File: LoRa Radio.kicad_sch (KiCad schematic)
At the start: 19 parts, among them U10 SX1262IMLTRT, U5 SKY66105, U9 74LVC2T45DC, Y2 ATX-11-F-32.000MHZ-F05-T

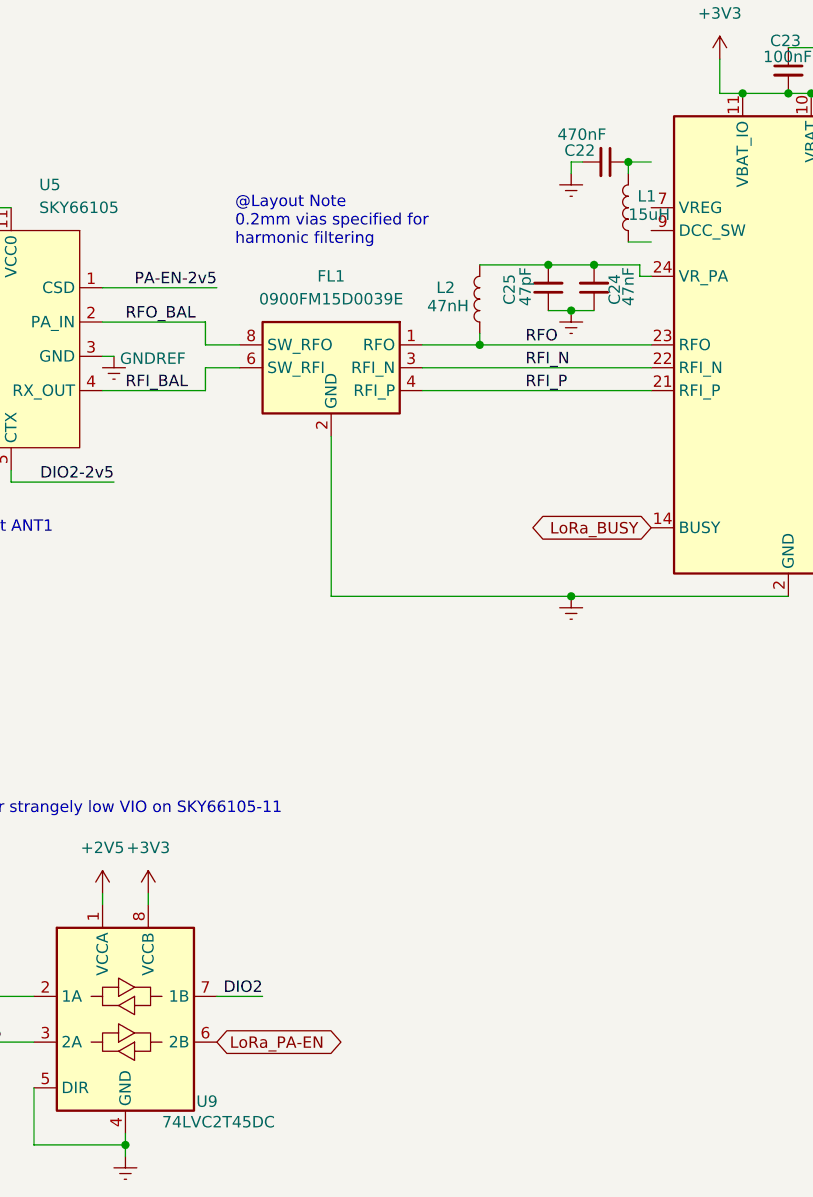
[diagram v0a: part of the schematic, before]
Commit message: Fix footprints and update rev number
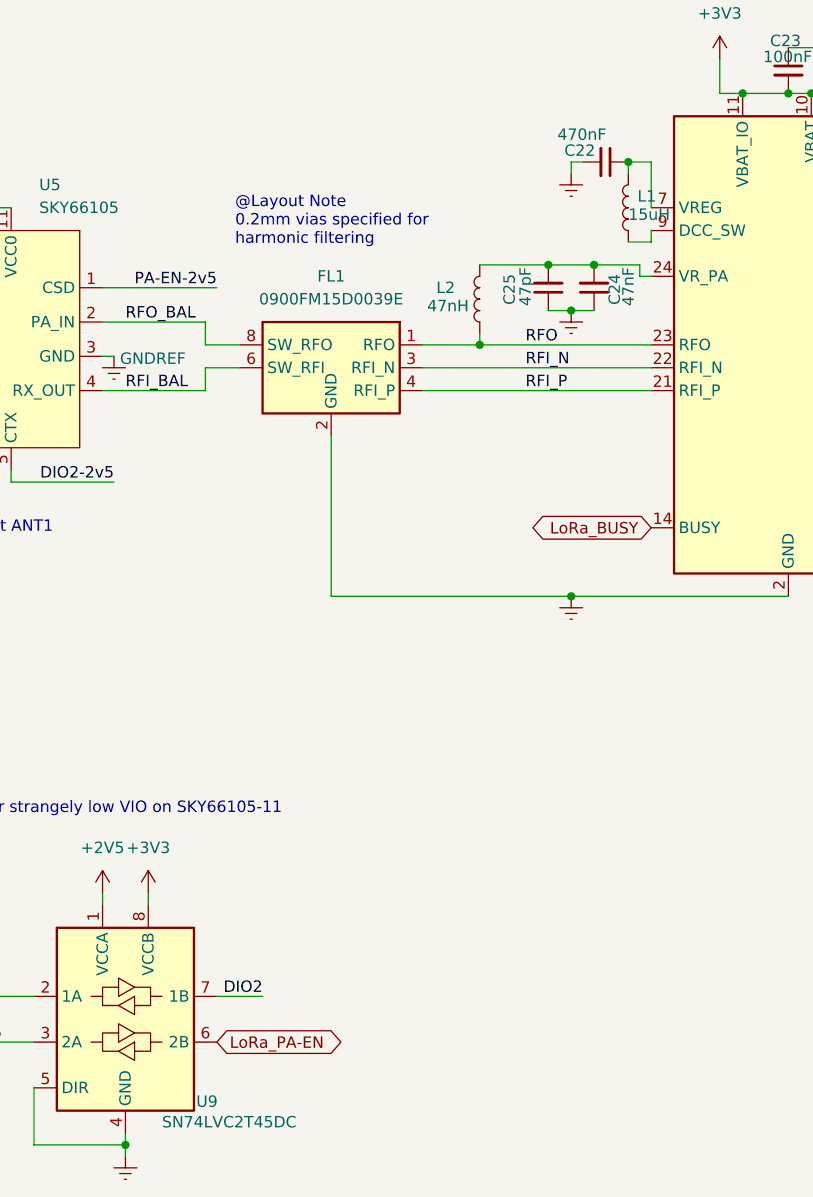
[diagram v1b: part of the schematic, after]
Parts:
- U9: value 74LVC2T45DC -> SN74LVC2T45DC; footprint Package_SO:VSSOP-8_2.3x2mm_P0.5mm -> Package_SO:MSOP-8_3x3mm_P0.65mm
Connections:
- net at U10.7 (VREG): now also C22.1, L1.2
- net at U10.9 (DCC_SW): now also L1.1
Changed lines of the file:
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@@
 	(title_block
 		(title "WINTER 915MHz LoRa Radio")
-		(date "2025-01-06")
-		(rev "3.3")
+		(date "2025-08-28")
+		(rev "4-Dev")
 		(company "SparrowTheNerd")
 	)
@@
 	(wire
 		(pts
+			(xy 149.86 60.96) (xy 149.86 66.04)
+		)
+		(stroke
+			(width 0)
+			(type default)
+		)
+	)
+	(wire
+		(pts
 			(xy 68.58 153.67) (xy 81.28 153.67)
 		)
@@
 	(wire
 		(pts
+			(xy 149.86 68.58) (xy 149.86 69.85)
+		)
+		(stroke
+			(width 0)
+			(type default)
+		)
+	)
+	(wire
+		(pts
 			(xy 88.9 74.93) (xy 101.6 74.93)
 		)
@@
 			)
 		)
-		(property "Value" "74LVC2T45DC"
+		(property "Value" "SN74LVC2T45DC"
 			(at 95.504 167.64 0)
 			(effects
@@
 			)
 		)
-		(property "Footprint" "Package_SO:VSSOP-8_2.3x2mm_P0.5mm"
+		(property "Footprint" "Package_SO:MSOP-8_3x3mm_P0.65mm"
 			(at 91.44 177.8 0)
 			(effects

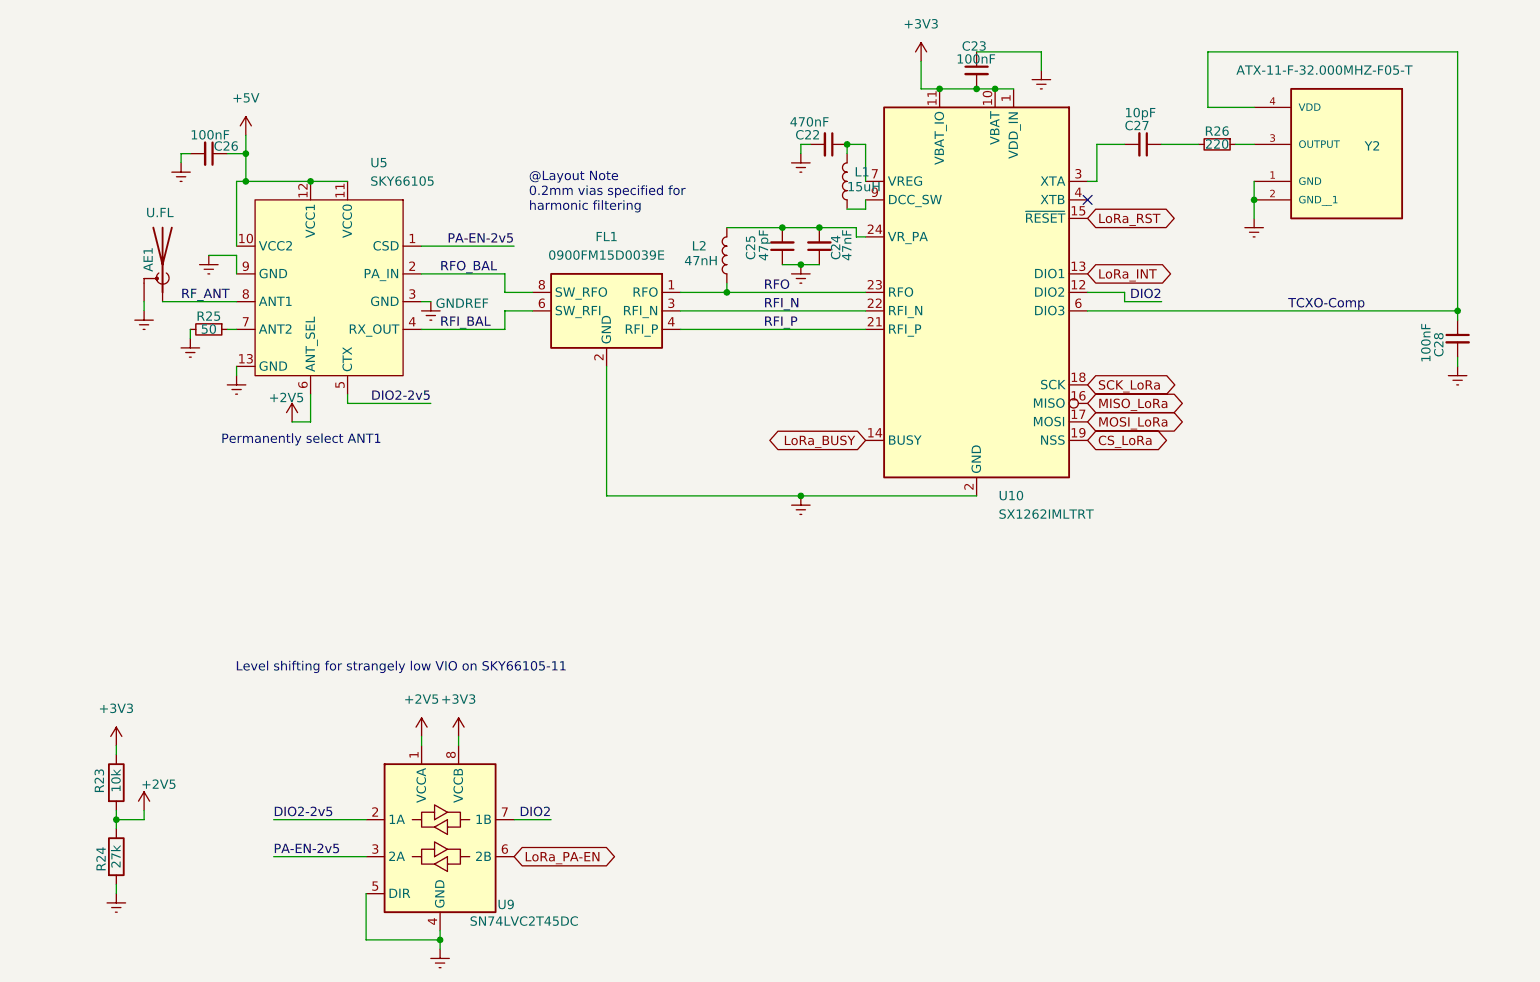
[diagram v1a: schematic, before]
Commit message: updated power delivery and component choices. v4 now ready
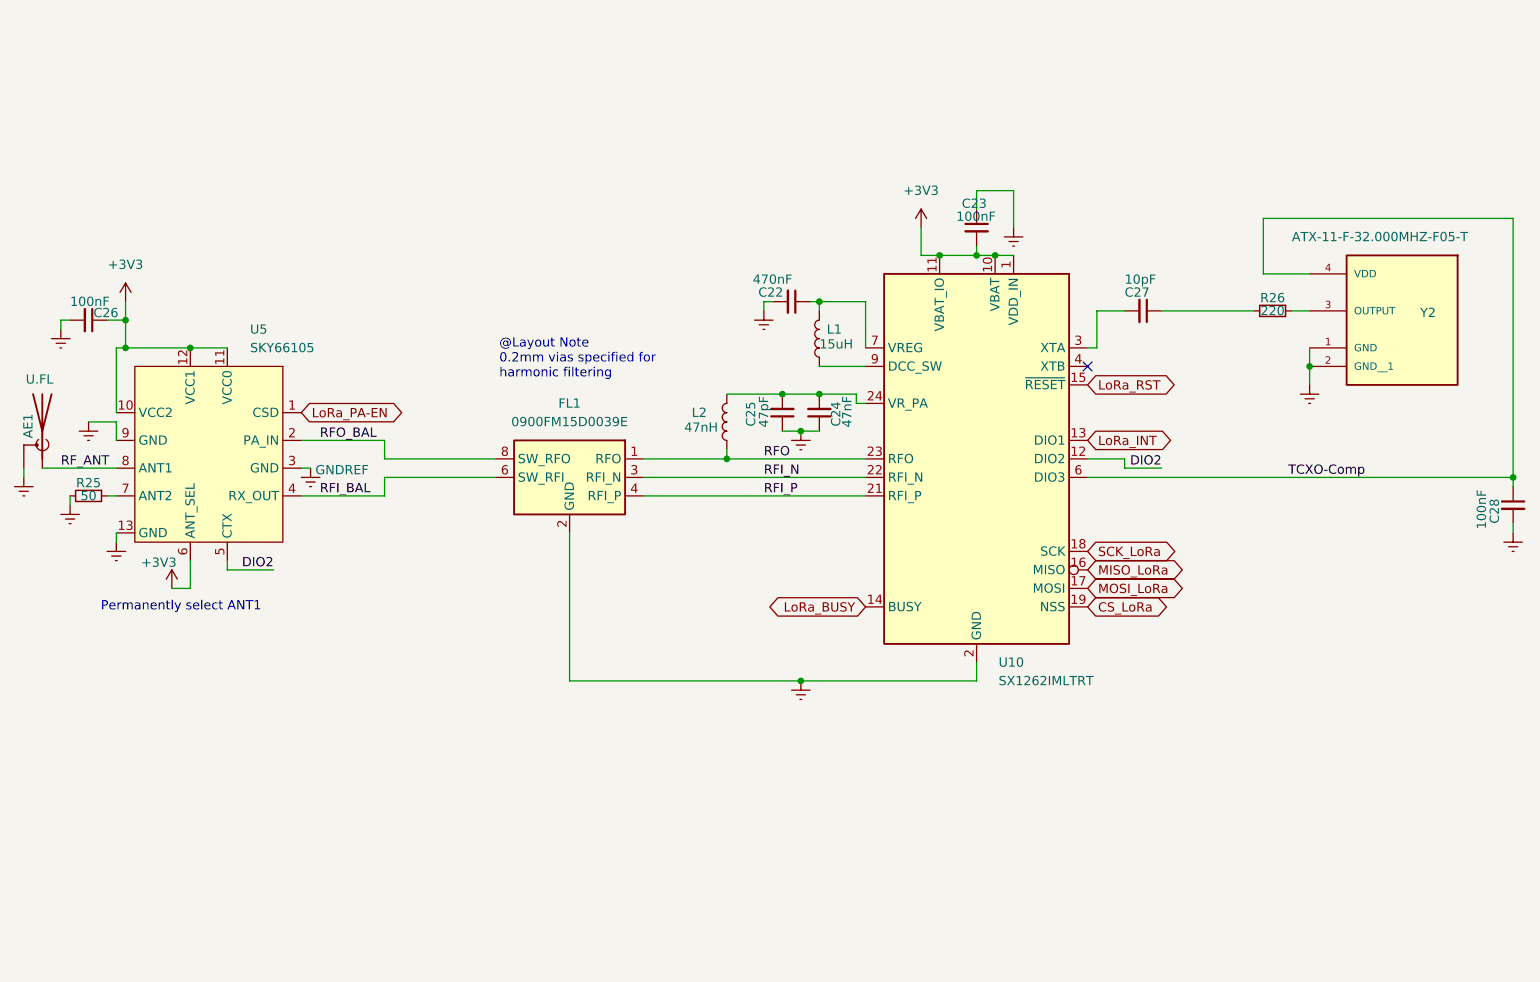
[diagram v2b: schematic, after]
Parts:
- removed R23: 10k, Resistor_SMD:R_0603_1608Metric, symbol Device:R
- removed R24: 27k, Resistor_SMD:R_0603_1608Metric, symbol Device:R
- removed U9: SN74LVC2T45DC, Package_SO:MSOP-8_3x3mm_P0.65mm, symbol Logic_LevelTranslator:74LVC2T45DC
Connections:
- net +2V5 is gone; now on net +3V3: U5.6 (ANT_SEL)
- net +5V is gone; now on net +3V3: C26.1, U5.10 (VCC2), U5.11 (VCC0), U5.12 (VCC1)
- net DIO2-2v5 is gone; now on net DIO2: U5.5 (CTX)
- net PA-EN-2v5 is gone; now on net LoRa_PA-EN: U5.1 (CSD)
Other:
- note removed: "Level shifting for strangely low VIO on SKY66105-11"
- moved on the sheet: AE1, C22, C23, C24, C25, C26, C27, C28, FL1, L1, L2, R25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

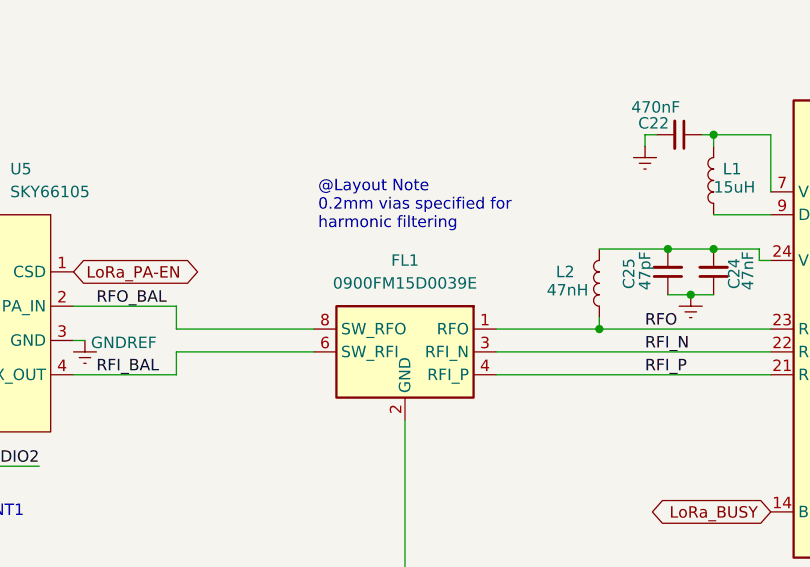
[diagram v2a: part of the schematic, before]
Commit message: Fixed power distribution and made small improvements. Updated revision number
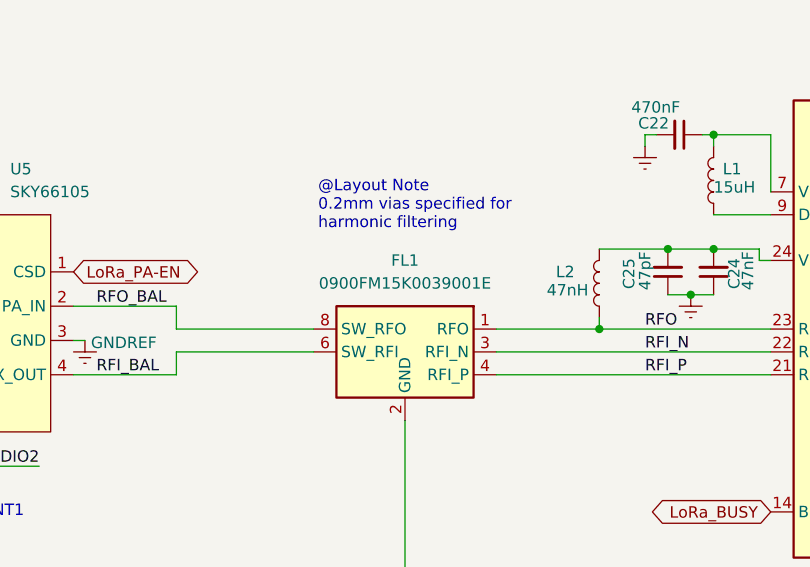
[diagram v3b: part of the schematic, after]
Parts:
- FL1: value 0900FM15D0039E -> 0900FM15K0039001E; Product ID 0900FM15D0039E -> 0900FM15K0039001E
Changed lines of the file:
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@@
 	(title_block
 		(title "WINTER 915MHz LoRa Radio")
-		(date "2025-08-28")
-		(rev "4-Dev")
+		(date "2025-11-24")
+		(rev "4.1")
 		(company "SparrowTheNerd")
 	)
@@
 			)
 		)
-		(property "Value" "0900FM15D0039E"
+		(property "Value" "0900FM15K0039001E"
 			(at 109.22 99.06 0)
 			(effects
@@
 			)
 		)
-		(property "Product ID" "0900FM15D0039E"
+		(property "Product ID" "0900FM15K0039001E "
 			(at 109.22 106.68 0)
 			(effects
